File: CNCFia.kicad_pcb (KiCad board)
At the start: 2 copper layers, 83.8 x 102.9 mm, 72 parts, among them J1 GND, J10 Driver_X, J11 Driver_Y, J12 Driver_Z, J13 Coolant, J14 Spin_10V, J15 Spin_Enabl, J16 Spin_Dir, J17 Mist, J2 EXT_5V, J3 Limit SW_XY, J4 Limit SW_ZA, J5 Extra SW 0, J6 Extra SW 1, J7 EXT_12V, J8 OPTO_5V, J9 Signal Input, Q1 2N3904, Q2 2N3904, Q3 2N3904, Q4 2N3904, U1 LTV-847, U2 LTV-847, U3 4504, U4 4504, U5 LM358P, U6 24LC16

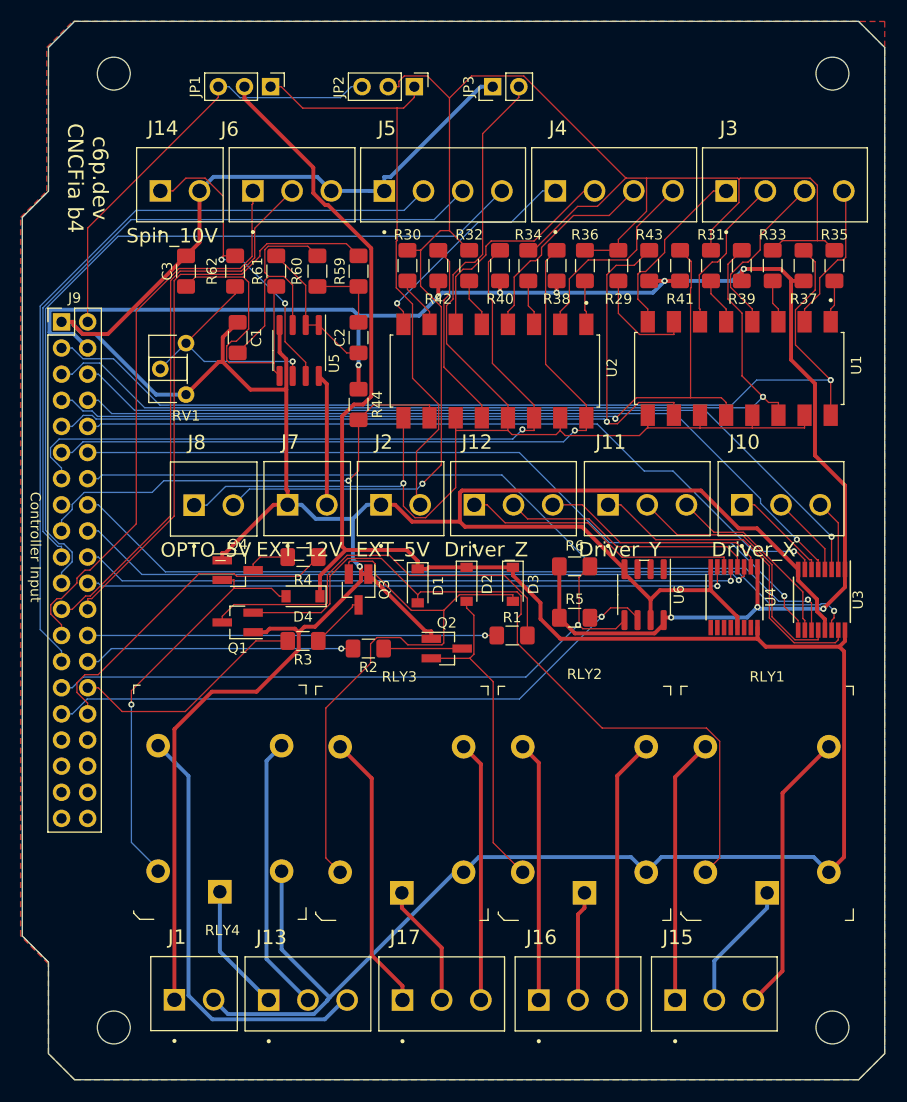
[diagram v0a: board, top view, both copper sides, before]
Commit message: Changed wrong GND for limit switches
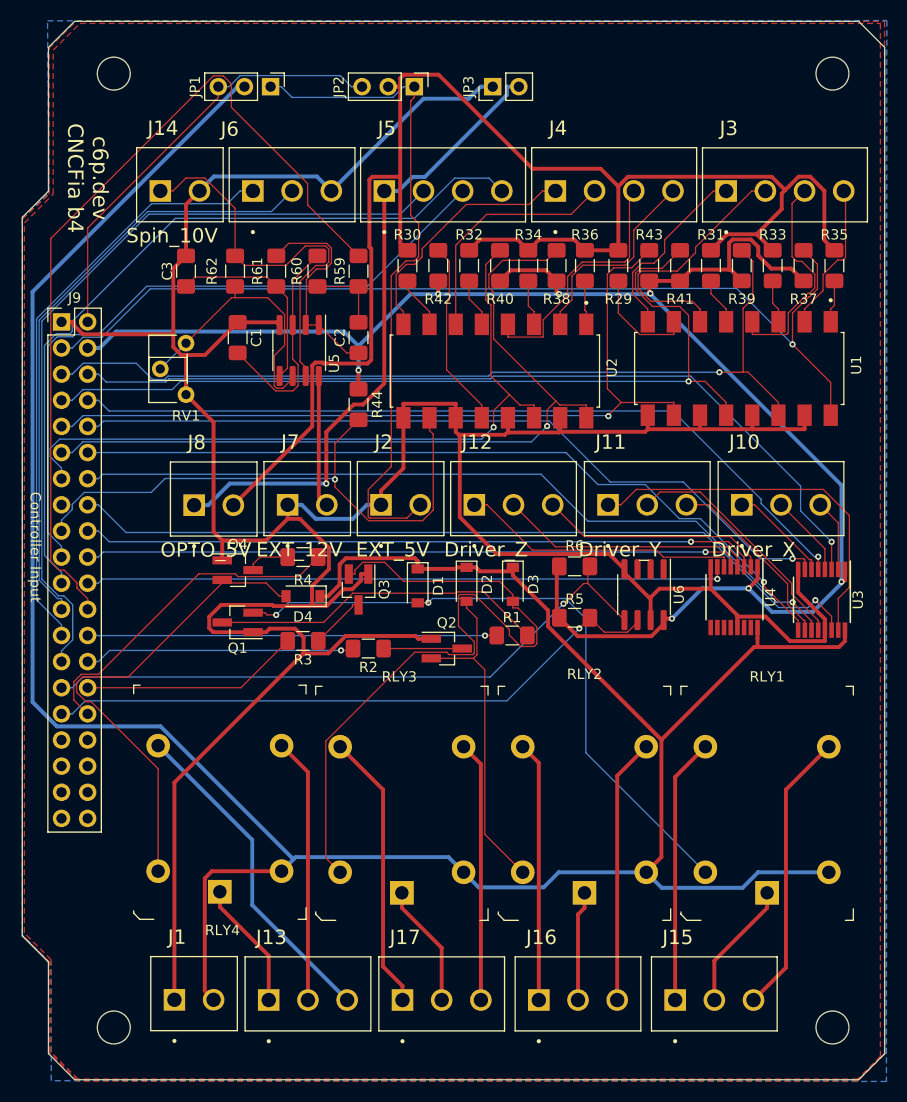
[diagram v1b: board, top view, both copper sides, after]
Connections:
- J5 pad 1: GND -> OPTO_GND
- U1 pad 11: OPTO_GND -> GND
- U1 pad 13: OPTO_GND -> GND
- U1 pad 15: OPTO_GND -> GND
- U1 pad 9: OPTO_GND -> GND
- U2 pad 11: OPTO_GND -> GND
- U2 pad 13: OPTO_GND -> GND
- U2 pad 15: OPTO_GND -> GND
- U2 pad 9: OPTO_GND -> GND
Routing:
- net OPTO_GND: track 123.6 -> 62.8 mm
- net GND: track 289.6 -> 331.6 mm, vias 1 -> 0
- net +5V: track 219.1 -> 260.7 mm
- net Spin_PWM: track 55.9 -> 84.1 mm
- net Net-(D3-Pad2): track 56.5 -> 71.9 mm
- net Extra_SW: track 45.9 -> 57.6 mm
- net /Relay_NC_4: track 42.5 -> 32.3 mm
- net Net-(C3-Pad1): track 28.8 -> 19.0 mm
- net /SW_YMIN: track 15.7 -> 25.5 mm
- net Net-(D1-Pad2): track 74.0 -> 64.4 mm, vias 0 -> 2
- net EXT_5V: track 57.1 -> 65.2 mm
- net /OUT_Spn_10V_0: track 30.6 -> 38.3 mm, vias 2 -> 0
- net Net-(C2-Pad1): track 14.2 -> 21.3 mm
- net Net-(Q1-Pad3): track 39.6 -> 32.6 mm
- net Net-(D4-Pad2): track 40.1 -> 47.1 mm, vias 1 -> 0
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- added copper zone on F.Cu, net +3V3

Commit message: Change mosfets and resistors to arrays
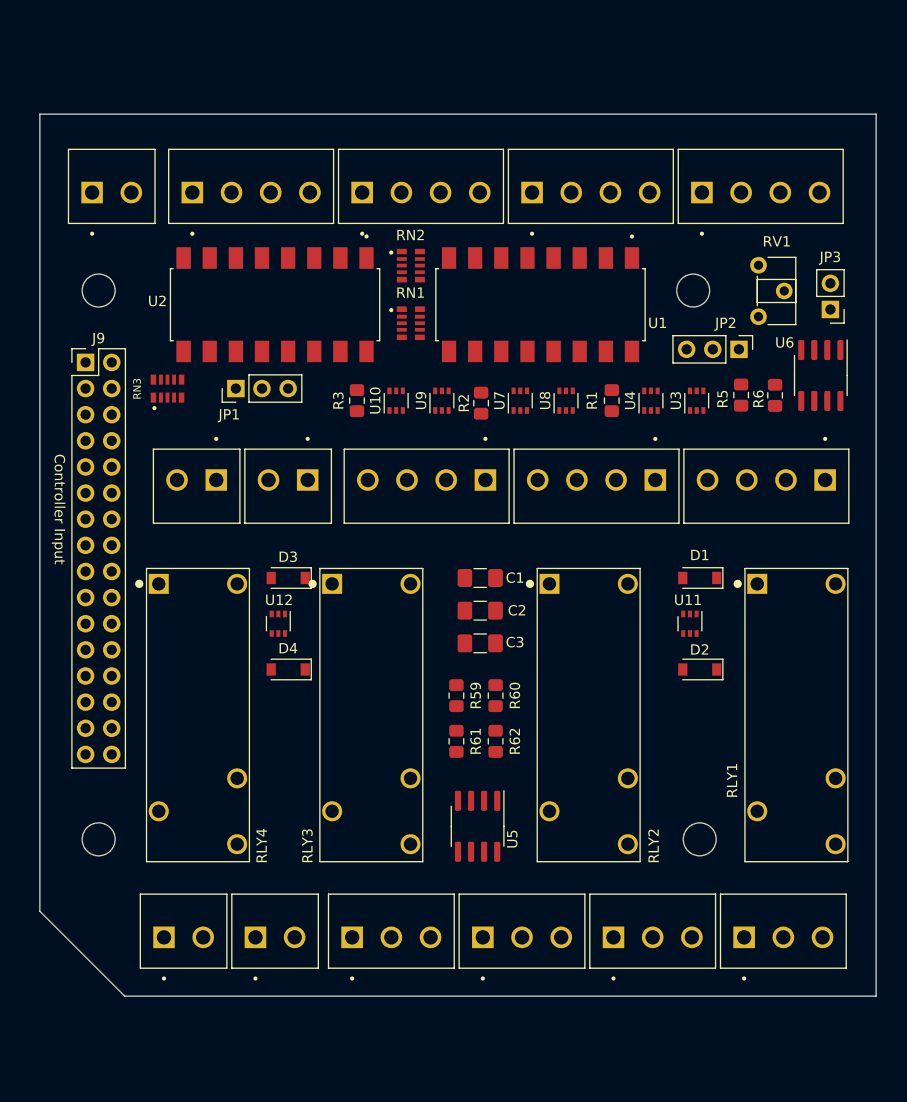
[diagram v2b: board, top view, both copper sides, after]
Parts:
- removed MH1, MH2, MH3, MH4: MountingHole_3.2mm_M3, MountingHole:MountingHole_3.2mm_M3
- removed Q1, Q2, Q3, Q4: 2N3904, Package_TO_SOT_SMD:SOT-23_Handsoldering
- removed R29, R30, R31, R32, R33, R34, R35, R36: 220R, Resistor_SMD:R_1206_3216Metric_Pad1.42x1.75mm_HandSolder
- removed R37, R38, R39, R40, R41, R42, R43, R44: 4K7, Resistor_SMD:R_1206_3216Metric_Pad1.42x1.75mm_HandSolder
- removed R4: 2k2, Resistor_SMD:R_1206_3216Metric_Pad1.42x1.75mm_HandSolder
- added M1: MountingHole_3.2mm_M3, MountingHole:MountingHole_3.2mm_M3, F.Cu at (45.5, 73.2)
- added M2: MountingHole_3.2mm_M3, MountingHole:MountingHole_3.2mm_M3, F.Cu at (103.3, 73.2)
- added M3: MountingHole_3.2mm_M3, MountingHole:MountingHole_3.2mm_M3, F.Cu at (103.9, 126.5)
- added M4: MountingHole_3.2mm_M3, MountingHole:MountingHole_3.2mm_M3, F.Cu at (45.5, 126.5)
- added RN1: CAY17-472JALF, Kicad_extra_components:RESCAXS64P320X160X60-10N, F.Cu at (75.9, 76.3)
- added RN2: CAY17-221JALF, Kicad_extra_components:RESCAXS64P320X160X60-10N, F.Cu at (75.9, 70.7)
- added RN3: CAY17-472JALF, Kicad_extra_components:RESCAXS64P320X160X60-10N, F.Cu at (52.2, 82.7)
- added U10: NTJD5121N, Package_TO_SOT_SMD:SOT-363_SC-70-6, F.Cu at (74.4, 83.9)
- added U11: NTJD5121N, Package_TO_SOT_SMD:SOT-363_SC-70-6, F.Cu at (103.0, 105.5)
- added U12: NTJD5121N, Package_TO_SOT_SMD:SOT-363_SC-70-6, F.Cu at (63.0, 105.5)
- added U7: NTJD5121N, Package_TO_SOT_SMD:SOT-363_SC-70-6, F.Cu at (86.5, 83.9)
- added U8: NTJD5121N, Package_TO_SOT_SMD:SOT-363_SC-70-6, F.Cu at (90.9, 83.9)
- added U9: NTJD5121N, Package_TO_SOT_SMD:SOT-363_SC-70-6, F.Cu at (78.9, 83.9)
- J1: value GND -> 5V_OUT
- J10, J11, J12: footprint Kicad_extra_components:CUI_TBP02R2-381-03BE -> Kicad_extra_components:CUI_TBP02R2-381-04BE
- J2: value EXT_5V -> IN_EXT_5V
- J6: value Extra SW 1 -> Extra SW 0; footprint Kicad_extra_components:CUI_TBP02R2-381-03BE -> Kicad_extra_components:CUI_TBP02R2-381-04BE
- J7: value EXT_12V -> IN_EXT_12V
- J8: value OPTO_5V -> IN_OPTO_PWR
- J9: footprint Connector_PinHeader_2.54mm:PinHeader_2x20_P2.54mm_Vertical -> Connector_PinHeader_2.54mm:PinHeader_2x16_P2.54mm_Vertical
- R1, R2, R3: value 2k2 -> 10k; footprint Resistor_SMD:R_1206_3216Metric_Pad1.42x1.75mm_HandSolder -> Kicad_extra_components:R_0805_2012Metric_Pad1.15x1.40mm_HandSolder
- R5, R59, R6, R60, R61, R62: footprint Resistor_SMD:R_1206_3216Metric_Pad1.42x1.75mm_HandSolder -> Kicad_extra_components:R_0805_2012Metric_Pad1.15x1.40mm_HandSolder
- RLY1, RLY2, RLY3, RLY4: value G5LE-14_DC5 -> G6RL-1 DC5; footprint digikey-footprints:Relay_THT_G5LE-14 -> Kicad_extra_components:RELAY_G6RL-1_5VDC
- U3, U4: value 4504 -> NTJD5121N; footprint Package_SO:TSSOP-16_4.4x5mm_P0.65mm -> Package_TO_SOT_SMD:SOT-363_SC-70-6
- moved J14 72.6 mm to (51.9, 136.0)
- moved RV1 57.0 mm to (109.7, 70.7), turned to 0 degrees
- moved R62 52.2 mm to (84.1, 117.0)
- moved U5 49.4 mm to (82.3, 125.2)
- moved R61 48.9 mm to (80.3, 117.0)
- moved C3 46.1 mm to (82.6, 107.4), turned to 180 degrees
- moved R60 44.7 mm to (84.1, 112.5)
- moved R59 42.3 mm to (80.3, 112.5)
- moved JP2 40.6 mm to (107.8, 78.9)
- moved JP3 39.3 mm to (116.6, 75.0), turned to 180 degrees
- moved C1 33.2 mm to (82.6, 101.1), turned to 0 degrees
- moved J8 32.0 mm to (44.9, 63.6)
- moved RLY3 30.8 mm to (68.2, 101.7), turned to -90 degrees
- moved RLY4 30.5 mm to (51.4, 101.7), turned to -90 degrees
- moved RLY2 30.2 mm to (89.3, 101.7), turned to -90 degrees
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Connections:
- net /HV_3 renamed /X_Dir-
- J10 pad 2: /HV_2 -> /X_Pulse-
- J10 pad 3: /HV_1 -> /X_Enable-
- J11 pad 1: /HV_6 -> /Y_Dir-
- J11 pad 2: /HV_5 -> /Y_Pulse-
- J11 pad 3: /HV_4 -> /Y_Enable-
- J12 pad 1: /HV_9 -> /Z_Dir-
- J12 pad 2: /HV_8 -> /Z_Pulse-
- J12 pad 3: /HV_7 -> /Z_Enable-
- J5 pad 1: OPTO_GND -> Feed_Hold
- J5 pad 2: Feed_Hold -> Reset
- J5 pad 3: Reset -> Door
- J5 pad 4: Door -> OPTO_GND
- J6 pad 1: Cycle_Start -> GND
- J6 pad 2: E_Stop -> GND
- J6 pad 3: GND -> E_Stop
- R1 pad 1: Net-(Q1-Pad3) -> +5V
- R1 pad 2: Spin_Enbl -> Net-(R1-Pad2)
- R2 pad 1: Net-(Q2-Pad3) -> +5V
- R2 pad 2: Spin_Dir -> Net-(R2-Pad2)
- R3 pad 1: Net-(Q3-Pad3) -> +5V
- R3 pad 2: Mist -> Net-(R3-Pad2)
- U2 pad 12: /Opto-isolated switches/e -> Probe
- U3 pad 1: +3V3 -> GND
- U3 pad 2: /HV_1 -> X_Dir
- U3 pad 3: X_Enbl -> /X_Pulse-
- U3 pad 4: /HV_2 -> GND
- U3 pad 5: X_Dir -> X_Step
- U4 pad 1: +3V3 -> GND
- U4 pad 2: /HV_7 -> X_Enbl
- U4 pad 3: Z_Enbl -> /X_Enable-
- U4 pad 4: /HV_8 -> GND
- U4 pad 5: Z_Dir -> Net-(R1-Pad2)
- U4 pad 6: /HV_9 -> Net-(R1-Pad2)
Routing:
- net GND: track 331.6 -> 0.00 mm
- net +5V: track 260.7 -> 0.00 mm
- net +3V3: track 171.9 -> 0.00 mm, vias 7 -> 0
- net OPTO_5V: track 150.9 -> 0.00 mm
- net LIM_XMin: track 94.9 -> 0.00 mm, vias 1 -> 0
- net LIM_YMin: track 86.9 -> 0.00 mm, vias 1 -> 0
- net LIM_XMax: track 86.2 -> 0.00 mm, vias 1 -> 0
- net Spin_PWM: track 84.1 -> 0.00 mm
- net X_Enbl: track 83.6 -> 0.00 mm, vias 1 -> 0
- net LIM_YMax: track 79.9 -> 0.00 mm, vias 1 -> 0
- net X_Dir: track 78.8 -> 0.00 mm, vias 1 -> 0
- net Y_Step: track 78.7 -> 0.00 mm, vias 1 -> 0
- net LIM_ZMin: track 78.0 -> 0.00 mm, vias 1 -> 0
- net Feed_Hold: track 77.4 -> 0.00 mm
- net Y_Dir: track 77.4 -> 0.00 mm, vias 1 -> 0
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- removed copper zone on B.Cu, net +3V3
- removed copper zone on F.Cu, net +3V3
- removed copper zone on F.Cu, net GND
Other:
- board size 83.8 x 102.9 mm -> 81.3 x 85.7 mm
- board text removed: "c6p.dev CNCFia b4"

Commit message: Made it more neat and organized
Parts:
- moved D1 2.62 mm to (103.3, 103.6)
- moved D2 2.62 mm to (103.3, 112.5)
- moved U11 2.62 mm to (102.4, 108.1)
- moved D3 2.54 mm to (63.9, 103.6)
- moved D4 2.54 mm to (63.9, 112.5)
- moved U12 2.54 mm to (63.0, 108.1)
- moved C2 1.27 mm to (82.6, 105.5)
- moved C3 1.27 mm to (82.6, 108.7)
- moved C1 1.27 mm to (82.6, 102.4)
- moved R59 1.27 mm to (80.3, 113.8)
- moved R60 1.27 mm to (84.1, 113.8)
- moved R61 1.27 mm to (80.3, 118.2)
- moved R62 1.27 mm to (84.1, 118.2)
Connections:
- J13 pad 1: /Relay_COM_4 -> /Relay_NC_4
- J13 pad 2: /Relay_NO_4 -> /Relay_COM_4
- J13 pad 3: /Relay_NC_4 -> /Relay_NO_4
- J14 pad 1: /OUT_Spn_10V_0 -> GND
- J14 pad 2: GND -> /OUT_Spn_10V_0
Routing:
- net GND: track 0.00 -> 233.0 mm, vias 0 -> 22
- net +5V: track 0.00 -> 204.5 mm
- net E_SCL: track 0.00 -> 94.5 mm, vias 0 -> 1
- net +3V3: track 0.00 -> 89.0 mm
- net E_SDA: track 0.00 -> 88.2 mm, vias 0 -> 1
- net Door: track 0.00 -> 85.5 mm, vias 0 -> 1
- net Feed_Hold: track 0.00 -> 81.9 mm, vias 0 -> 1
- net LIM_XMin: track 0.00 -> 80.4 mm, vias 0 -> 1
- net OPTO_GND: track 0.00 -> 76.6 mm
- net Net-(R62-Pad2): track 0.00 -> 76.5 mm, vias 0 -> 1
- net Cycle_Start: track 0.00 -> 76.1 mm, vias 0 -> 1
- net OPTO_5V: track 0.00 -> 69.8 mm, vias 0 -> 1
- net E_Stop: track 0.00 -> 68.1 mm
- net LIM_XMax: track 0.00 -> 67.9 mm, vias 0 -> 1
- net +12V: track 0.00 -> 66.1 mm
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- added copper zone on F.Cu, net +5V
- added copper zone on B.Cu, net GND
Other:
- board text added: "+12V"
- board text added: "+5V"
- board text added: "+V"
- board text added: "12V IN"
- board text added: "5V"
- board text added: "5V Output"
- board text added: "5V SOURCE"
- board text added: "COM"
- board text added: "CYCLE START"
- board text added: "Coolant Relay"
- board text added: "DIR-"
- board text added: "DOOR SAFETY"
- board text added: "EMERG STOP"
- board text added: "ENA-"
- board text added: "EXT 5V"
- board text added: "EXTERNAL"
- board text added: "EXTERNAL 5V IN"
- board text added: "EXTRA"
- board text added: "FEED HOLD"
- board text added: "GND"
- board text added: "MCU"
- board text added: "Mist Coolant Relay"
- board text added: "NC"
- board text added: "NO"
- board text added: "OPTO 5V IN"
- board text added: "OPTO 5V SOURCE"
- board text added: "OPTO GND"
- board text added: "OPTO GND SOURCE"
- board text added: "PROBE"
- board text added: "PUL-"
- board text added: "RESET"
- board text added: "SPINDLE V TUNING"
- board text added: "SWITCHES"
- board text added: "Spindle Analog"
- board text added: "Spindle Direction"
- board text added: "Spindle Enable"
- board text added: "X DRIVER"
- board text added: "X MAX"
- board text added: "X MIN"
- board text added: "Y DRIVER"
- board text added: "Y MAX"
- board text added: "Y MIN"
- board text added: "Z DRIVER"
- board text added: "Z MAX"
- board text added: "Z MIN"

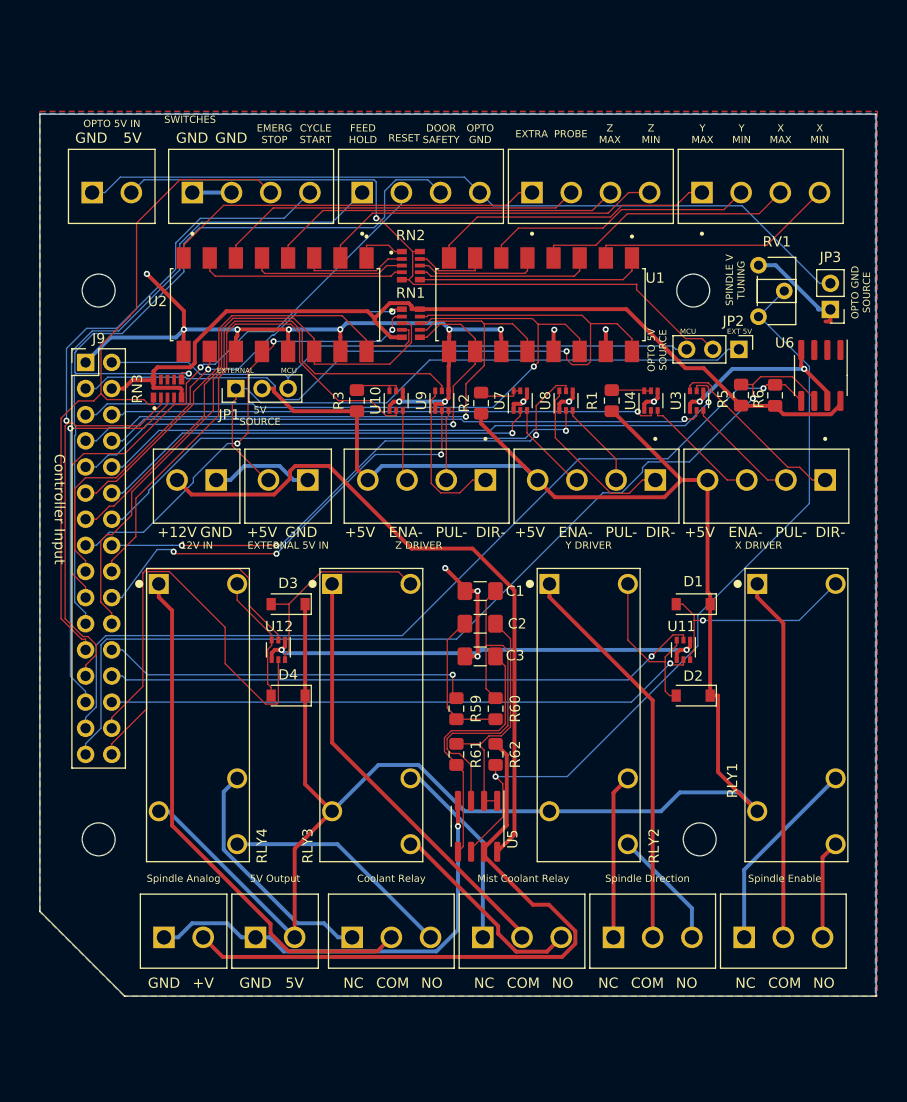
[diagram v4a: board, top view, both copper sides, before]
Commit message: Simplify the power options
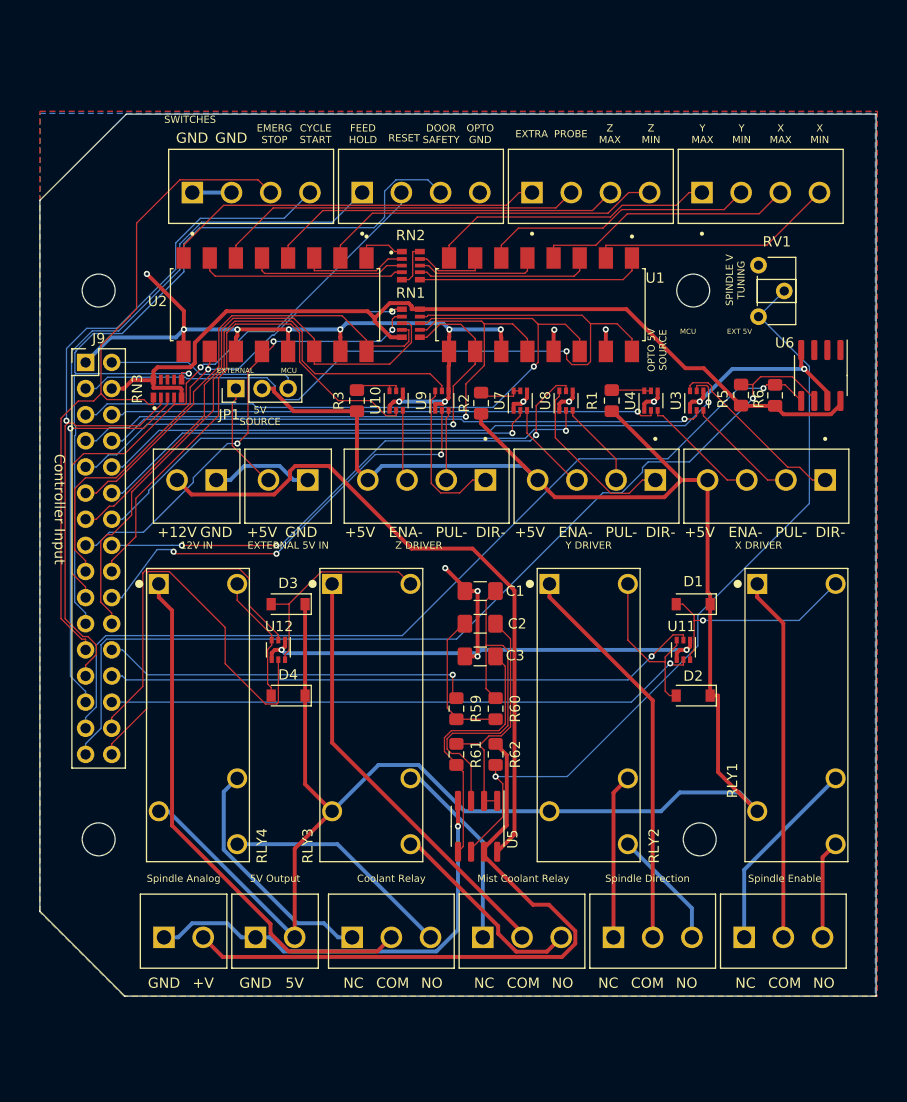
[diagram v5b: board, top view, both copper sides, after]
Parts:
- removed J8: IN_OPTO_PWR, Kicad_extra_components:CUI_TBP02R2-381-02BE
- removed JP2: Opto_V_Source, Connector_PinHeader_2.54mm:PinHeader_1x03_P2.54mm_Vertical
- removed JP3: Opto_GND_Source, Connector_PinHeader_2.54mm:PinHeader_1x02_P2.54mm_Vertical
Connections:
- J5 pad 4: OPTO_GND -> Net-(J5-Pad4)
- RN2 pad 10: OPTO_5V -> +5V
- RN2 pad 5: OPTO_5V -> +5V
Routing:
- net OPTO_GND: track 76.6 -> 0.00 mm
- net OPTO_5V: track 69.8 -> 0.00 mm, vias 1 -> 0
- net EXT_5V: track 62.0 -> 10.4 mm
- net MCU_5V: track 59.0 -> 18.8 mm
- net GND: track 233.0 -> 222.5 mm
- net +5V: track 204.5 -> 208.7 mm
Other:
- outline, holes or cut-outs redrawn
- board text removed: "OPTO 5V IN"
- board text removed: "OPTO GND SOURCE"

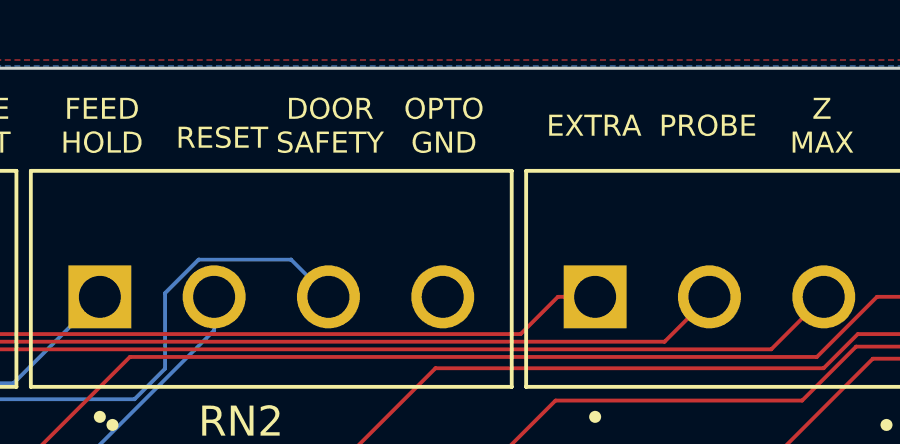
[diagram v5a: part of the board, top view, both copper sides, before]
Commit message: Simplify the power options again
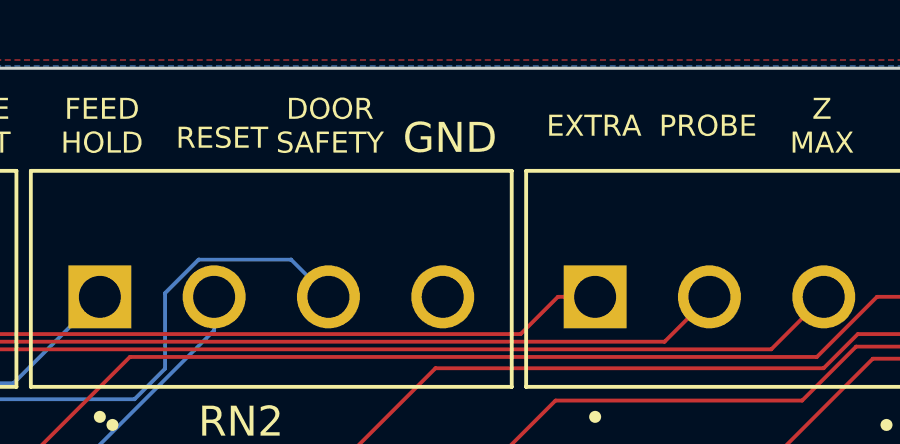
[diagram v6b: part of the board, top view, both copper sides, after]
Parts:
- RLY2, RLY3, RLY4: value G6RL-1 DC5 -> G6RL-1 DC5
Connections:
- J5 pad 4: Net-(J5-Pad4) -> GND
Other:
- board text removed: "OPTO GND"
